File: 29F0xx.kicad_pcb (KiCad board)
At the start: 2 copper layers, 50.2 x 55.9 mm, 8 parts, among them J1 TL866 Adapter Left, J2 Extra Pins, J3 Willem_ZIF_DIP32, J4 TL866 Adapter Right

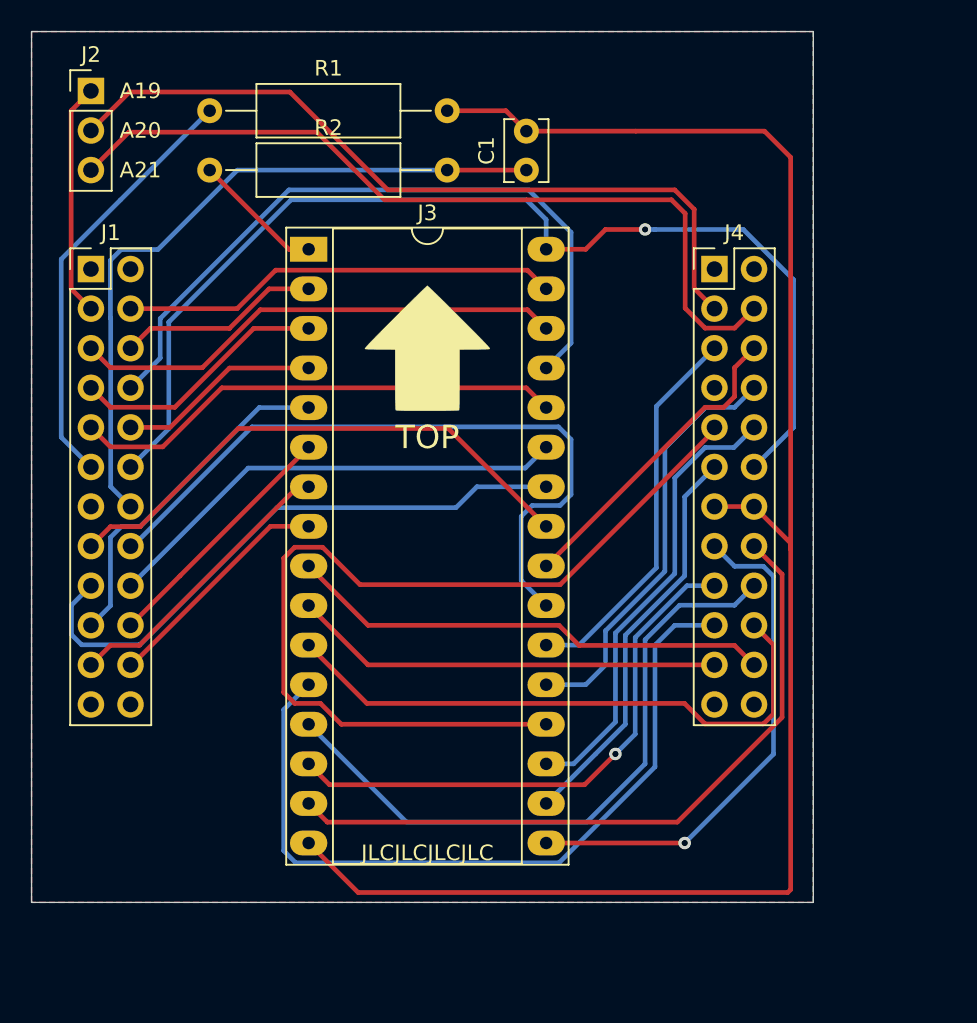
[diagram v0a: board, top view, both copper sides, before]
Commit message: Redo with looser tolerances
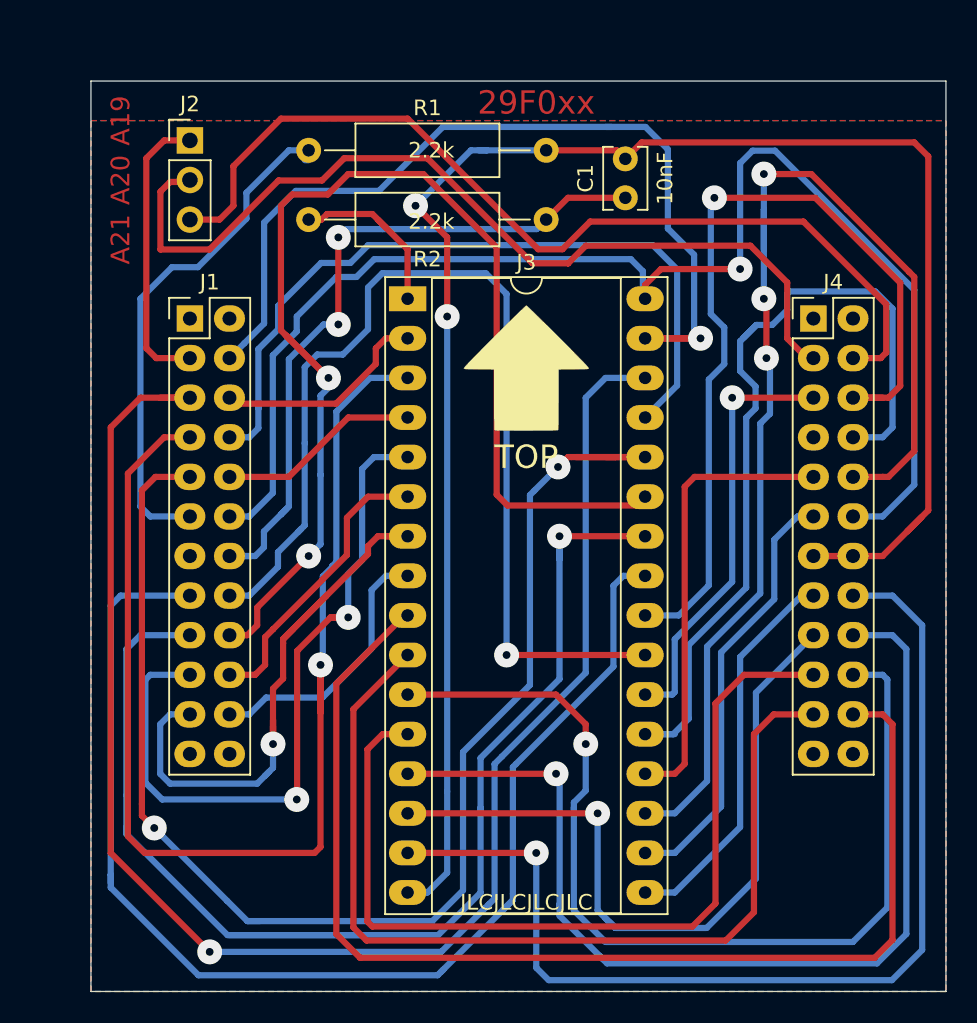
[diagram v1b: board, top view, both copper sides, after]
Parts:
- J1: footprint Connector_PinHeader_2.54mm:PinHeader_2x12_P2.54mm_Vertical -> Willem:PinHeader_2x12_P2.54mm_Vertical
- moved J2 7.10 mm to (29.2, 24.8)
- moved J1 7.10 mm to (29.2, 36.2)
- moved J3 7.10 mm to (43.2, 34.9)
- moved J4 7.10 mm to (69.2, 36.2)
- moved R2 7.10 mm to (36.8, 29.8)
- moved R1 6.84 mm to (36.8, 25.4)
- moved C1 6.59 mm to (57.1, 28.4)
- moved G*** 6.48 mm to (50.8, 39.4)
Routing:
- net /A17: track 31.8 -> 102.7 mm, vias 0 -> 1
- net /A15: track 16.6 -> 78.6 mm, vias 0 -> 1
- net /A13: track 31.8 -> 90.0 mm, vias 0 -> 2
- net /A9: track 38.6 -> 87.5 mm, vias 0 -> 1
- net /A8: track 30.4 -> 78.6 mm, vias 0 -> 2
- net /D5: track 29.2 -> 76.3 mm, vias 0 -> 3
- net /A11: track 34.9 -> 80.2 mm
- net /A3: track 31.2 -> 75.9 mm
- net /~OE: track 20.2 -> 56.7 mm, vias 0 -> 1
- net /A2: track 27.6 -> 61.5 mm
- net /A18: track 28.2 -> 58.9 mm, vias 0 -> 1
- net /D6: track 59.5 -> 29.3 mm
- net /D7: track 27.1 -> 55.3 mm
- net /A1: track 38.4 -> 63.8 mm, vias 0 -> 1
- net /A7: track 22.3 -> 47.0 mm, vias 0 -> 2
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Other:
- board size 50.2 x 55.9 mm -> 54.9 x 58.4 mm
- net class Default: clearance 0.25 -> 0.5; trace_width 0.3 -> 0.4; via_dia 0.8 -> 1.6; via_drill 0.4 -> 0.5
- rule pad_to_mask_clearance: 0 -> 0.1
- rule trace_clearance: 0.25 -> 0.5
- board text added: "29F0xx"
